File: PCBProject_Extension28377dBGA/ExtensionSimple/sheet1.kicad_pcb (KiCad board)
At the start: 4 copper layers, 118 parts, among them J1 HIF3FC-20PA-2.54DSA, J17 HIF3FC-20PA-2.54DSA, J2 HIF3FC-20PA-2.54DSA, J3 HIF3FC-20PA-2.54DSA, P1 TMS320F28377D-BGA-Core, P10 Header 2X2, P11 Header 2X2, P12 Header 2X2, P13 Header 6X2, P14 Header 6X2, P19 Header 2X2, P2 Header 6X2, P20 Header 2X2, P21 Header 2X2, P22 Header 2X2, P9 Header 2X2, Q2 FMMT618TA, U1 SN74HC365D, U2 SN74ABT541, U3 SN74ABT541

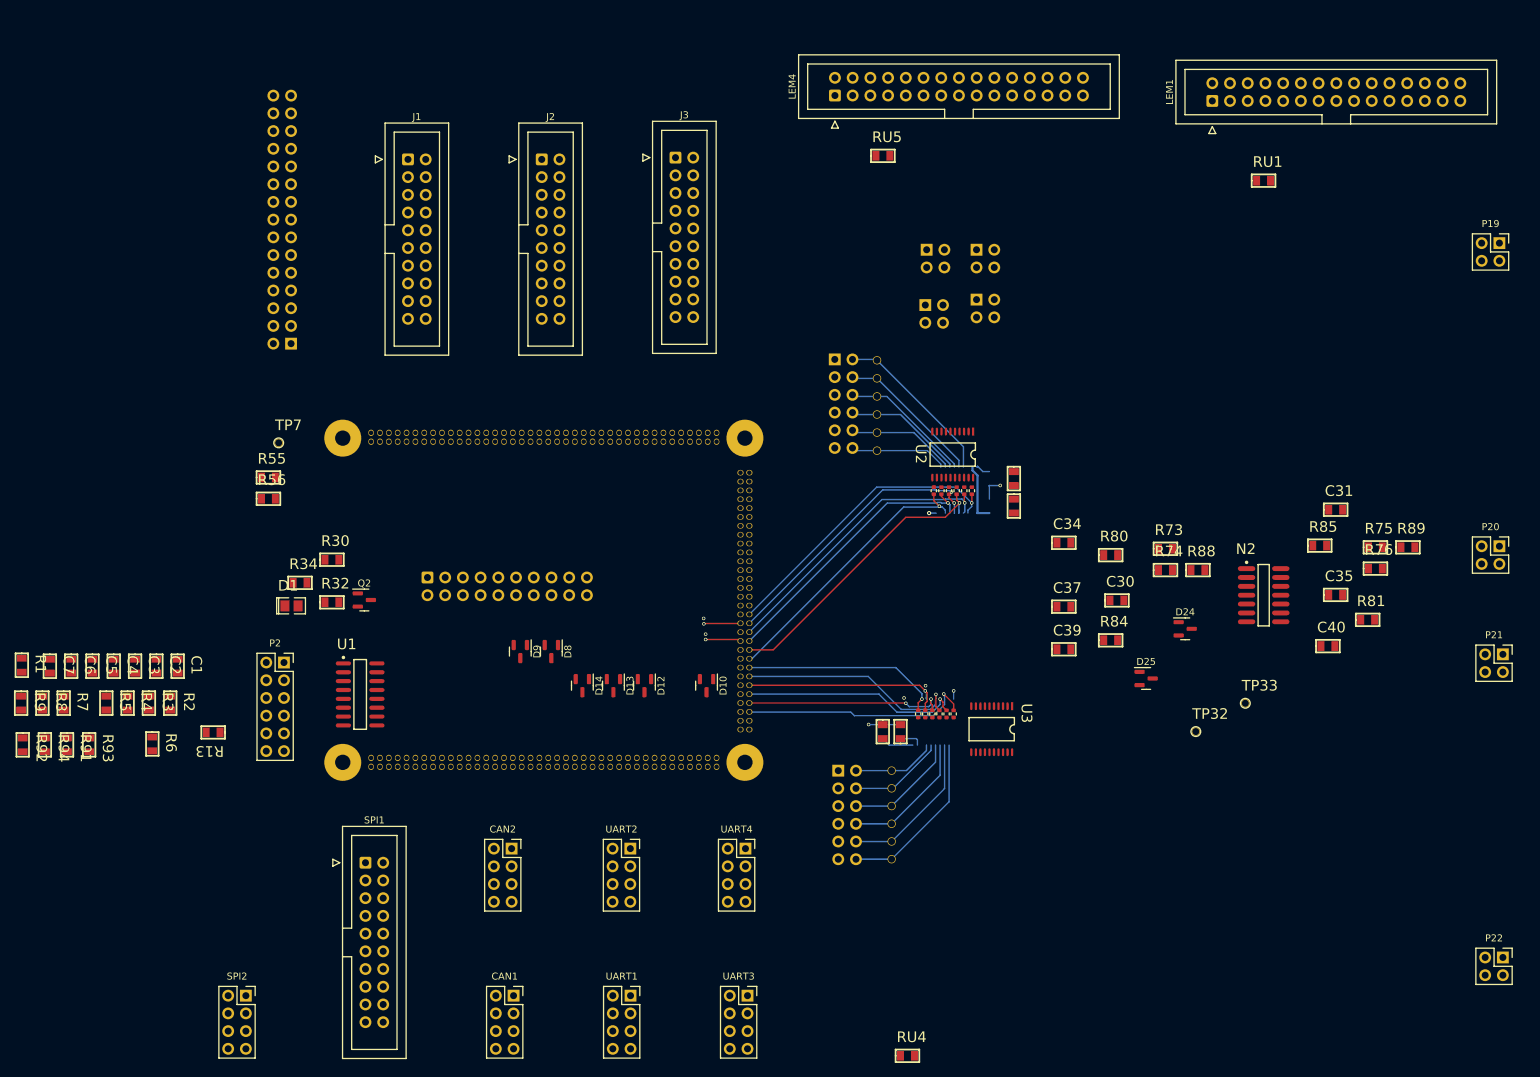
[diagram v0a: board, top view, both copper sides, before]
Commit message: fix bugs in power and LEM boards
12VGND should be negative input to amp on LEM. May be also need single connected?
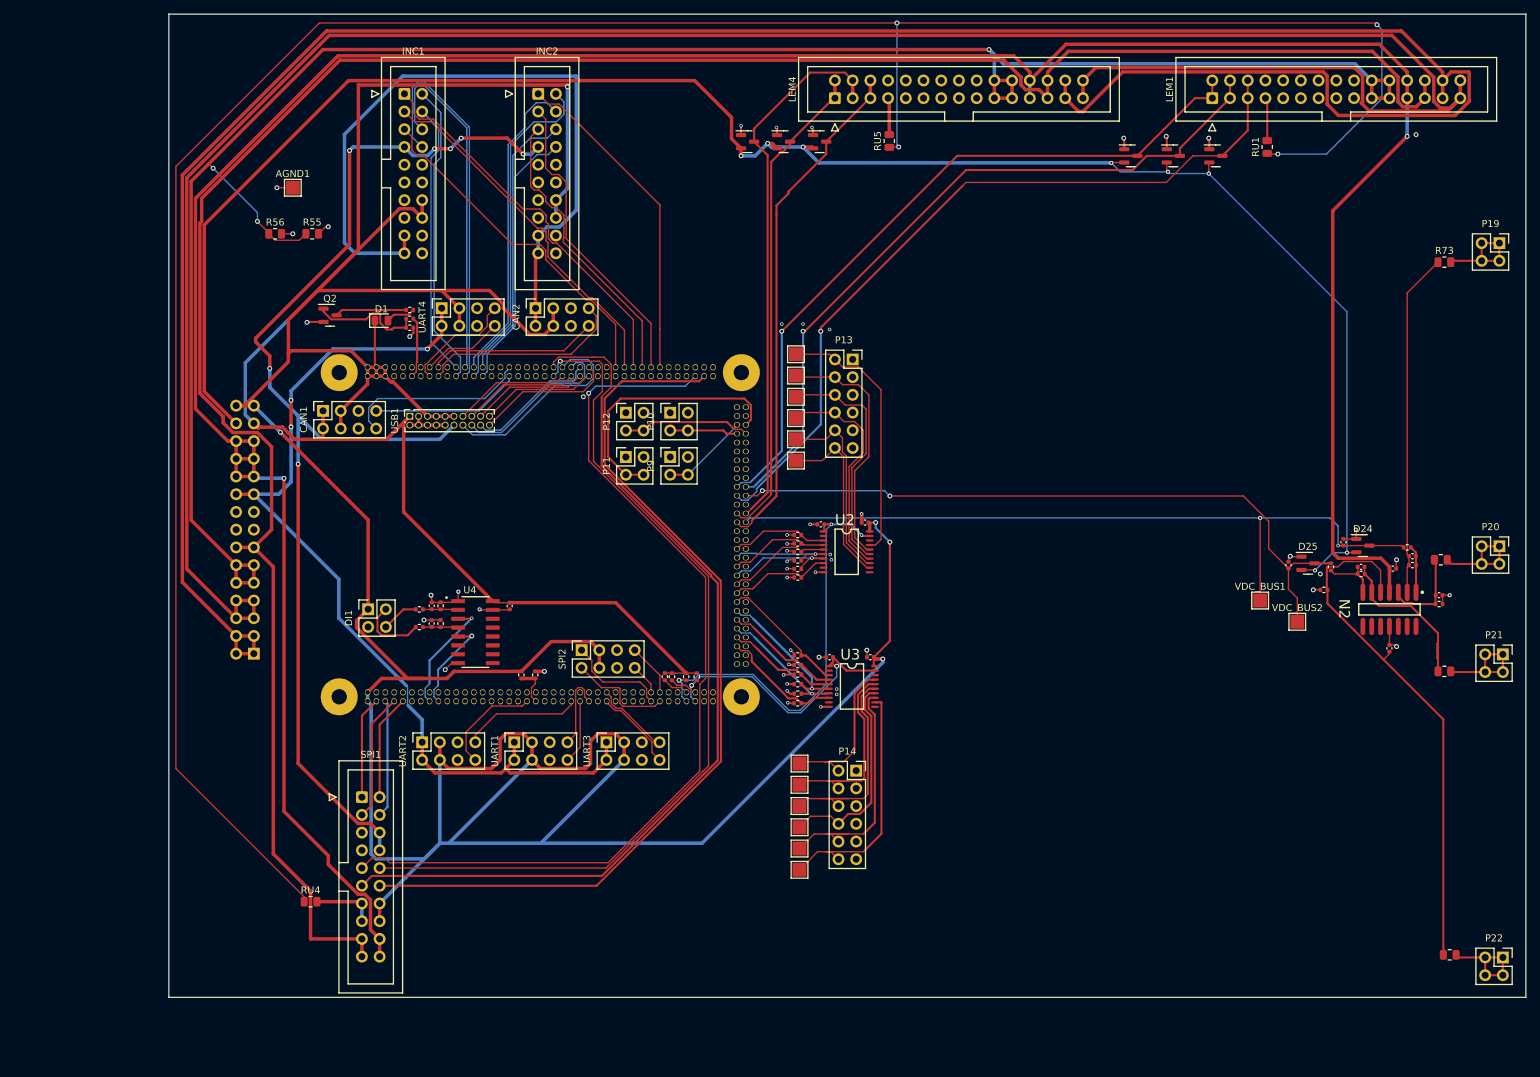
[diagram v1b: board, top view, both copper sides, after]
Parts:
- removed C1, C3, C5: 101, mmlab-footprint-library:0805
- removed C6: 103, mmlab-footprint-library:0805
- removed J17, J3: HIF3FC-20PA-2.54DSA, Connector_IDC:IDC-Header_2x10_P2.54mm_Vertical
- removed P2: Header 6X2, Connector_PinSocket_2.54mm:PinSocket_2x06_P2.54mm_Vertical
- removed R3, R4, R5, R7: 1K, mmlab-footprint-library:0805
- removed TP32, TP33: TP-黄色测试点, mmlab-footprint-library:TESTPOINT-TH_BD1.0
- removed U1: SN74HC365D, mmlab-footprint-library:D016_N
- added DI1: Conn_02x02_Counter_Clockwise, Connector_PinSocket_2.54mm:PinSocket_2x02_P2.54mm_Vertical, F.Cu at (194.2, 148.8)
- added U4: SN74HC365D, 1mmlab_footprint:SOIC127P600X175-16N, F.Cu at (209.6, 152.1)
- added USB1: HIF3FC-20PA-2.54DSA, Connector_PinSocket_1.27mm:PinSocket_2x10_P1.27mm_Vertical, F.Cu at (200.2, 121.2)
- added VDC_BUS1: TP-黄色测试点, TestPoint:TestPoint_Pad_2.0x2.0mm, F.Cu at (322.1, 147.6)
- added VDC_BUS2: TP-黄色测试点, TestPoint:TestPoint_Pad_2.0x2.0mm, F.Cu at (327.4, 150.6)
- AGND1: renamed from TP7; footprint mmlab-footprint-library:TESTPOINT-TH_BD1.0 -> TestPoint:TestPoint_Pad_2.0x2.0mm
- C2, C25, C26, C30, C31, C34, C35, C37, C39, C4, C40, C7, C8, C9: footprint mmlab-footprint-library:0805 -> Capacitor_SMD:C_0402_1005Metric
- D1: footprint mmlab-footprint-library:L0805 -> LED_SMD:LED_0805_2012Metric
- N2: footprint mmlab-footprint-library:SOIC14_M -> 1mmlab_footprint:SOIC14_M
- P1: footprint mmlab-footprint-library:DSP_240 -> 1mmlab_footprint:DSP_240
- P10, P11, P12, P13, P14, P9: moved to F.Cu
- R1, R13, R2, R30, R32, R34, R6, R8, R80, R81, R84, R85, R88, R89, R9, R91, R92, R93, R94: footprint mmlab-footprint-library:0805 -> Resistor_SMD:R_0402_1005Metric
- R55, R56, R73, R74, R75, R76, RU1, RU4, RU5: footprint mmlab-footprint-library:0805 -> Resistor_SMD:R_0805_2012Metric
- TP11, TP12, TP15, TP16, TP19, TP20, TP23, TP24, TP27, TP28, TP5, TP6: footprint mmlab-footprint-library:TESTPOINT-TH_BD1.0 -> TestPoint:TestPoint_Pad_2.0x2.0mm; moved to F.Cu
- U2, U3: footprint mmlab-footprint-library:TSSOP-20 -> 1mmlab_footprint:TSSOP-20
- moved D12 111.7 mm to (315.7, 83.8), turned to 0 degrees
- moved D13 110.5 mm to (309.6, 83.8), turned to 0 degrees
- moved D14 109.3 mm to (303.5, 83.8), turned to 0 degrees
- moved R92 97.1 mm to (241.3, 158.5), turned to 90 degrees
- moved R94 90.4 mm to (237.7, 158.5)
- moved R91 89.3 mm to (239.8, 158.5), turned to 90 degrees
- moved UART4 88.9 mm to (204.7, 105.7), turned to 90 degrees
- moved RU4 88.4 mm to (185.9, 190.8)
- moved CAN1 88.2 mm to (187.7, 120.4), turned to 90 degrees
- moved R93 83.1 mm to (236.7, 158.5)
- moved D8 82.6 mm to (258.9, 81.8), turned to 0 degrees
- moved D9 80.0 mm to (248.6, 81.8), turned to 0 degrees
- moved D10 78.8 mm to (253.7, 81.8), turned to 0 degrees
- moved CAN2 77.6 mm to (218.2, 105.7), turned to 90 degrees
- moved SPI2 69.1 mm to (224.8, 154.7), turned to 90 degrees
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- renumbered J1 to INC1, J2 to INC2
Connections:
- P1 pad 105: /DSP_PWM4_~{FAULT} -> unconnected-(P1-105_D4-Pad105)
- P1 pad 106: unconnected-(P1-A8_106-Pad106) -> /DSP_PWM4_~{FAULT}
- P1 pad 107: /DSP_PWM3_~{FAULT} -> unconnected-(P1-107_D3-Pad107)
- P1 pad 108: unconnected-(P1-A7_108-Pad108) -> /DSP_PWM3_~{FAULT}
- P1 pad 109: /DSP_PWM2_~{FAULT} -> unconnected-(P1-109_D2-Pad109)
- P1 pad 11: /LED1 -> /LED2
- P1 pad 110: unconnected-(P1-A6_110-Pad110) -> /DSP_PWM2_~{FAULT}
- P1 pad 111: /DSP_PWM1_~{FAULT} -> unconnected-(P1-111_D1-Pad111)
- P1 pad 112: unconnected-(P1-A5_112-Pad112) -> /DSP_PWM1_~{FAULT}
- P1 pad 117: /UART_SCI_TXDB -> unconnected-(P1-117_GP137-Pad117)
- P1 pad 118: unconnected-(P1-A2_118-Pad118) -> /UART_SCI_TXDB
- P1 pad 119: /BootFromFlash -> unconnected-(P1-119_GP84-Pad119)
- P1 pad 12: /LED2 -> /LED1
- P1 pad 120: unconnected-(P1-A1_120-Pad120) -> /BootFromFlash
- P1 pad 127: /UART_SCI_RXDB -> unconnected-(P1-127_GP138-Pad127)
- P1 pad 128: unconnected-(P1-GP113_128-Pad128) -> /UART_SCI_RXDB
- P1 pad 129: /UART_SCI_RXDA -> unconnected-(P1-129_GP136-Pad129)
- P1 pad 13: /LED3 -> /LED4
- P1 pad 130: unconnected-(P1-GP110_130-Pad130) -> /UART_SCI_RXDA
- P1 pad 131: /UART_SCI_TXDA -> unconnected-(P1-131_GP135-Pad131)
- P1 pad 132: unconnected-(P1-GP123_132-Pad132) -> /UART_SCI_TXDA
- P1 pad 135: /UART_SCI_RXDC -> /UART_SCI_TXDC
- P1 pad 136: /UART_SCI_TXDC -> /UART_SCI_RXDC
- P1 pad 14: /LED4 -> /LED3
- P1 pad 145: /SPI B MO HS -> /SPI_B_CK_HS
- P1 pad 146: /SPI_B_CK_HS -> /SPI B MO HS
- P1 pad 147: /SPI B MI HS -> /~{SPI_B_STE_HS}
- P1 pad 148: /~{SPI_B_STE_HS} -> /SPI B MI HS
- P1 pad 15: /UART_SCI_RXDD -> /UART_SCI_TXDD
- P1 pad 153: /DSP_PWM1~{_ENABL}E -> /DSP_PWM3~{_ENABL}E
- P1 pad 154: /DSP_PWM3~{_ENABL}E -> /DSP_PWM1~{_ENABL}E
- P1 pad 155: /DSP_PWM2~{_ENABL}E -> /DSP_PWM4~{_ENABL}E
- P1 pad 156: /DSP_PWM4~{_ENABL}E -> /DSP_PWM2~{_ENABL}E
- P1 pad 16: /UART_SCI_TXDD -> /UART_SCI_RXDD
- P1 pad 165: /AD_14 -> /AD_15
- P1 pad 166: /AD_15 -> /AD_14
- P1 pad 167: /ADD4 -> /ADD5
- P1 pad 168: /ADD5 -> /ADD4
- P1 pad 169: /IPM_IW3 -> /IPM_IV3
- P1 pad 17: /DSP_A_CAN_TX -> /DSP_A_CAN_RX
- P1 pad 170: /IPM_IV3 -> /IPM_IW3
- P1 pad 171: /IPM_IU3 -> /IPM_VDC_BUS3
- P1 pad 172: /IPM_VDC_BUS3 -> /IPM_IU3
- P1 pad 173: /IPM_IW4 -> /IPM_IV4
- P1 pad 174: /IPM_IV4 -> /IPM_IW4
- P1 pad 175: /IPM_IU4 -> /IPM_VDC_BUS4
- P1 pad 176: /IPM_VDC_BUS4 -> /IPM_IU4
- P1 pad 177: /IPM_Temperature2 -> /IPM_Temperature4
- P1 pad 178: /IPM_Temperature4 -> /IPM_Temperature2
- P1 pad 179: /IPM_IW2 -> /IPM_IV2
- P1 pad 18: /DSP_A_CAN_RX -> /DSP_A_CAN_TX
- P1 pad 180: /IPM_IV2 -> /IPM_IW2
- P1 pad 181: /IPM_IU2 -> /IPM_VDC_BUS2
- P1 pad 182: /IPM_VDC_BUS2 -> /IPM_IU2
- P1 pad 183: /IPM_Temperature1 -> /IPM_Temperature3
- P1 pad 184: /IPM_Temperature3 -> /IPM_Temperature1
- P1 pad 185: /IPM_IW1 -> /IPM_IV1
- P1 pad 186: /IPM_IV1 -> /IPM_IW1
- P1 pad 187: /IPM_IU1 -> /IPM_VDC_BUS1
- P1 pad 188: /IPM_VDC_BUS1 -> /IPM_IU1
- P1 pad 193: /DSP-PWM1A -> /DSP-PWM7A
- P1 pad 194: /DSP-PWM7A -> /DSP-PWM1A
- P1 pad 195: /DSP-PWM1B -> /DSP-PWM7B
- P1 pad 196: /DSP-PWM7B -> /DSP-PWM1B
- P1 pad 197: /DSP-PWM2A -> /DSP-PWM8A
- P1 pad 198: /DSP-PWM8A -> /DSP-PWM2A
- P1 pad 199: /DSP-PWM2B -> /DSP-PWM8B
- P1 pad 200: /DSP-PWM8B -> /DSP-PWM2B
- P1 pad 201: /DSP-PWM3A -> /DSP-PWM9A
- P1 pad 202: /DSP-PWM9A -> /DSP-PWM3A
- P1 pad 203: /DSP-PWM3B -> /DSP-PWM9B
- P1 pad 204: /DSP-PWM9B -> /DSP-PWM3B
- P1 pad 205: /DSP-PWM4A -> /DSP-PWM10A
- P1 pad 206: /DSP-PWM10A -> /DSP-PWM4A
- P1 pad 207: /DSP-PWM4B -> /DSP-PWM10B
- P1 pad 208: /DSP-PWM10B -> /DSP-PWM4B
- P1 pad 209: /DSP-PWM5A -> /DSP-PWM11A
- P1 pad 21: /MQEP1A -> /MQEP1B
- P1 pad 210: /DSP-PWM11A -> /DSP-PWM5A
- P1 pad 211: /DSP-PWM5B -> /DSP-PWM11B
- P1 pad 212: /DSP-PWM11B -> /DSP-PWM5B
- P1 pad 213: /DSP-PWM6A -> /DSP-PWM12A
- P1 pad 214: /DSP-PWM12A -> /DSP-PWM6A
- P1 pad 215: /DSP-PWM6B -> /DSP-PWM12B
- P1 pad 216: /DSP-PWM12B -> /DSP-PWM6B
- P1 pad 22: /MQEP1B -> /MQEP1A
- P1 pad 23: /MQEP1S -> /MQEP1Z
- P1 pad 24: /MQEP1Z -> /MQEP1S
- P1 pad 25: /MQEP2A -> /MQEP2B
- P1 pad 26: /MQEP2B -> /MQEP2A
- P1 pad 27: /MQEP2S -> /MQEP2Z
- P1 pad 28: /MQEP2Z -> /MQEP2S
- P1 pad 29: /MQEP3A -> /MQEP3B
- P1 pad 30: /MQEP3B -> /MQEP3A
- P1 pad 31: /MQEP3S -> /MQEP3Z
- P1 pad 32: /MQEP3Z -> /MQEP3S
- P1 pad 33: /DSP_B_CAN_TX -> /DSP_B_CAN_RX
- P1 pad 34: /DSP_B_CAN_RX -> /DSP_B_CAN_TX
- P1 pad 43: /~{SPI_A_STE_HS} -> /SPI_A_CK_HS
- P1 pad 44: /SPI_A_CK_HS -> /~{SPI_A_STE_HS}
- P1 pad 45: /MUSB_EN -> /MUSB_DM
- P1 pad 46: /MUSB_DM -> /MUSB_EN
- P1 pad 47: /MUSB_FLT -> /MUSB_ID
- P1 pad 48: /MUSB_ID -> /MUSB_FLT
- P1 pad 49: /MUSB_INT -> /MUSB_VB
- P1 pad 50: /MUSB_VB -> /MUSB_INT
- P1 pad 51: /MUSB_DP -> /MUSB_BZ
- P1 pad 52: /MUSB_BZ -> /MUSB_DP
- P1 pad 57: unconnected-(P1-57_GP30-Pad57) -> /QEP1_HALL_W
- P1 pad 58: /QEP1_HALL_W -> unconnected-(P1-GP17_58-Pad58)
- P1 pad 59: unconnected-(P1-59_GP57-Pad59) -> /QEP1_HALL_V
- P1 pad 60: /QEP1_HALL_V -> unconnected-(P1-GP94_60-Pad60)
- P1 pad 61: unconnected-(P1-61_GP66-Pad61) -> /QEP1_HALL_U
- P1 pad 62: /QEP1_HALL_U -> unconnected-(P1-GP68_62-Pad62)
- P1 pad 63: unconnected-(P1-63_GP131-Pad63) -> /QEP2_HALL_W
- P1 pad 64: /QEP2_HALL_W -> unconnected-(P1-GP67_64-Pad64)
- P1 pad 65: unconnected-(P1-65_GP116-Pad65) -> /QEP2_HALL_V
- P1 pad 66: /QEP2_HALL_V -> unconnected-(P1-GP32_66-Pad66)
- P1 pad 67: unconnected-(P1-67_GP127-Pad67) -> /QEP2_HALL_U
- P1 pad 68: /QEP2_HALL_U -> unconnected-(P1-GP115_68-Pad68)
- P1 pad 69: unconnected-(P1-69_GP128-Pad69) -> /QEP3_HALL_U
- P1 pad 70: /QEP3_HALL_U -> unconnected-(P1-GP117_70-Pad70)
- P1 pad 71: unconnected-(P1-71_GP126-Pad71) -> /QEP3_HALL_V
- P1 pad 72: /QEP3_HALL_V -> unconnected-(P1-GP130_72-Pad72)
- P1 pad 73: unconnected-(P1-73_GP95-Pad73) -> /QEP3_HALL_W
- P1 pad 74: /QEP3_HALL_W -> unconnected-(P1-GP54_74-Pad74)
- P1 pad 75: /SPI_A_MO_HS -> unconnected-(P1-75_GP58-Pad75)
- P1 pad 76: unconnected-(P1-GP56_76-Pad76) -> /SPI_A_MO_HS
- P1 pad 77: /SPI_A_MI_HS -> unconnected-(P1-77_GP59-Pad77)
- P1 pad 78: unconnected-(P1-GP55_78-Pad78) -> /SPI_A_MI_HS
- P1 pad 83: /SPI_C_MO_HS -> /ECAP1_IPM_TerminalDutyU1
- P1 pad 84: /ECAP1_IPM_TerminalDutyU1 -> /SPI_C_MO_HS
- P1 pad 85: /SPI_C_MI_HS -> /ECAP2_IPM_TerminalDutyV1
- P1 pad 86: /ECAP2_IPM_TerminalDutyV1 -> /SPI_C_MI_HS
- P1 pad 87: /SPI_C_CK_HS -> /ECAP3_IPM_TerminalDutyW1
- P1 pad 88: /ECAP3_IPM_TerminalDutyW1 -> /SPI_C_CK_HS
- P1 pad 89: /~{SPI_C_STE_HS} -> /ECAP4_IPM_TerminalDutyU2
- P1 pad 90: /ECAP4_IPM_TerminalDutyU2 -> /~{SPI_C_STE_HS}
- P1 pad 91: unconnected-(P1-91_D11-Pad91) -> /ECAP5_IPM_TerminalDutyV2
- P1 pad 92: /ECAP5_IPM_TerminalDutyV2 -> unconnected-(P1-A15_92-Pad92)
- P1 pad 93: unconnected-(P1-93_D10-Pad93) -> /ECAP6_IPM_TerminalDutyW2
- P1 pad 94: /ECAP6_IPM_TerminalDutyW2 -> unconnected-(P1-A14_94-Pad94)
- P1 pad 95: /DI-1-DSP-3.3V -> unconnected-(P1-95_D9-Pad95)
- P1 pad 96: unconnected-(P1-A13_96-Pad96) -> /DI-1-DSP-3.3V
- P1 pad 97: /DI-2-DSP-3.3V -> unconnected-(P1-97_D8-Pad97)
- P1 pad 98: unconnected-(P1-A12_98-Pad98) -> /DI-2-DSP-3.3V
- POWER1 pad 27: AVDD -> VDD
- R55 pad 1: D12VGND -> 12VGND
- R56 pad 1: D12VGND -> 12VGND
- SPI1 pad 17: -5V_ADC -> A-5V
- SPI1 pad 19: -5V_ADC -> A-5V
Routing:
- net D+5V: track 6.85 -> 560.8 mm, vias 0 -> 5
- net A+5V: track 0.00 -> 412.1 mm, vias 0 -> 2
- net +12: track 0.00 -> 352.7 mm
- net REF_3V: track 0.00 -> 343.8 mm, vias 0 -> 4
- net -12: track 0.00 -> 340.1 mm
- net A-5V: track 0.00 -> 329.4 mm
- net 12VGND: track 0.00 -> 291.6 mm, vias 0 -> 3
- net AVDD: track 0.00 -> 272.0 mm, vias 0 -> 8
- net VDD: track 0.00 -> 232.3 mm
- net PE_GND: track 0.00 -> 169.2 mm, vias 0 -> 7
- net D12V1: track 0.00 -> 133.8 mm, vias 0 -> 3
- net /SPI_A_MO_HS: track 0.00 -> 132.5 mm, vias 0 -> 1
- net /SPI_A_CK_HS: track 0.00 -> 132.5 mm
- net /SPI_A_MI_HS: track 0.00 -> 130.9 mm
- net /~{SPI_A_STE_HS}: track 0.00 -> 126.9 mm, vias 0 -> 1
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- added copper zone on In1.Cu, net AGND
- added copper zone on In2.Cu, net AGND
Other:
- board outline added: 194.6 x 141 mm
